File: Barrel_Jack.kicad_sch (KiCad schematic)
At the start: 24 parts, among them J10 Barrel_Jack, J11 Barrel_Jack, J12 Barrel_Jack, J13 Barrel_Jack, J14 Barrel_Jack, J6 Barrel_Jack, J8 Barrel_Jack, J9 Barrel_Jack, U19 34.81-9024, U20 34.81-9024, U21 34.81-9024, U22 34.81-9024, U23 34.81-9024, U24 34.81-9024, U25 34.81-9024, U26 34.81-9024

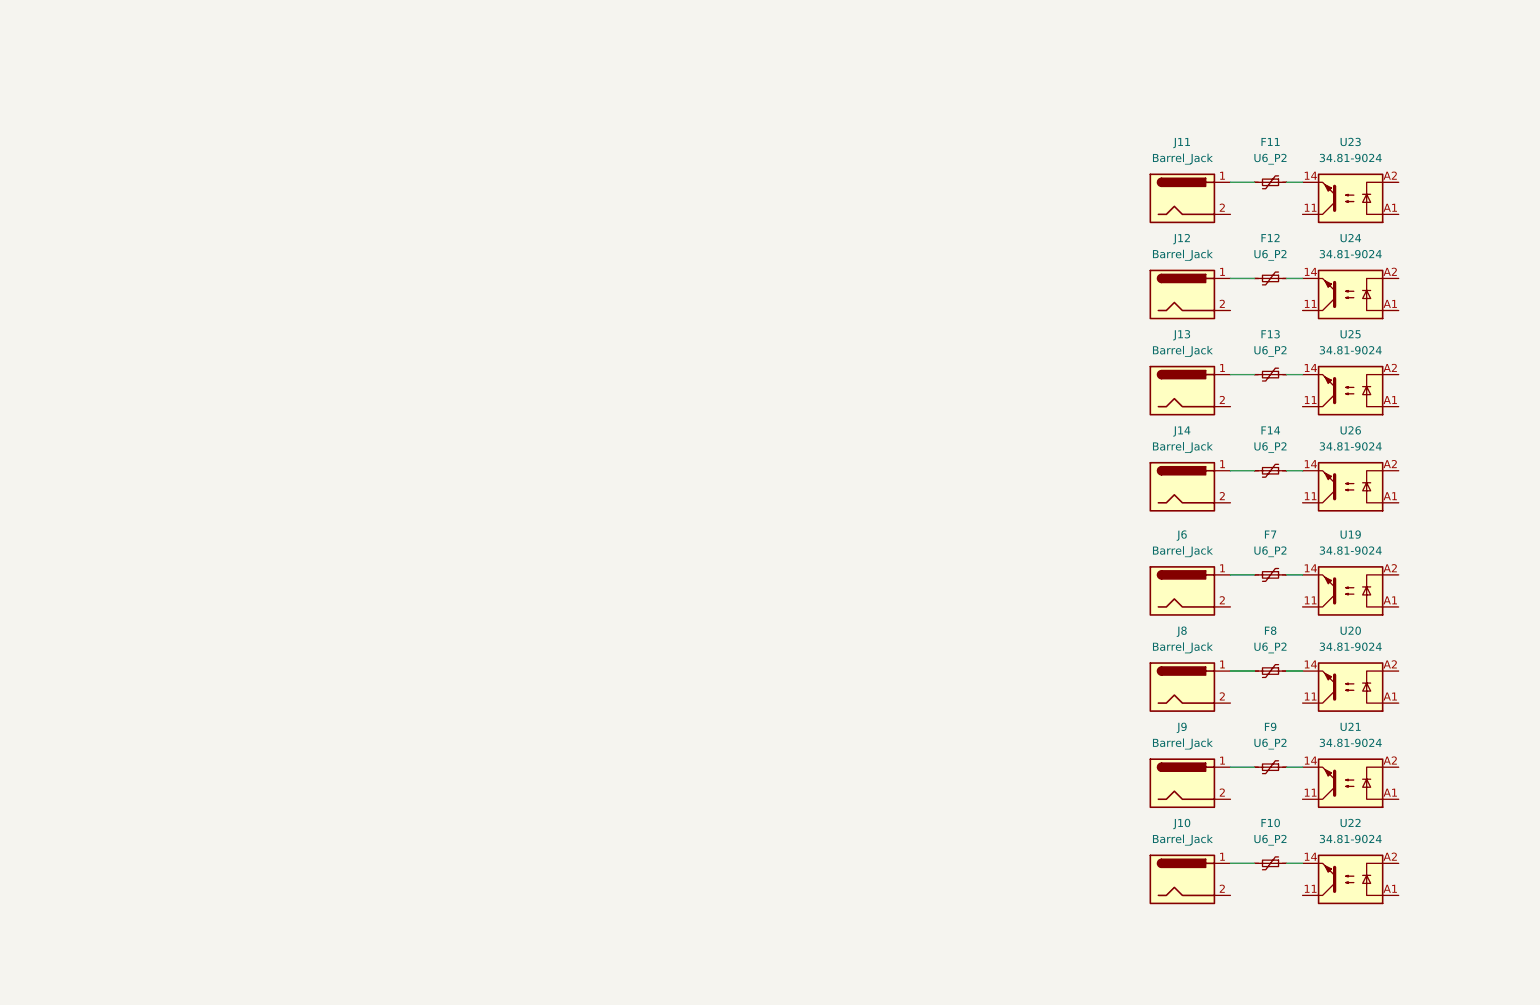
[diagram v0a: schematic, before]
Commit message: barrel jack multiple versions, should be turned into branches
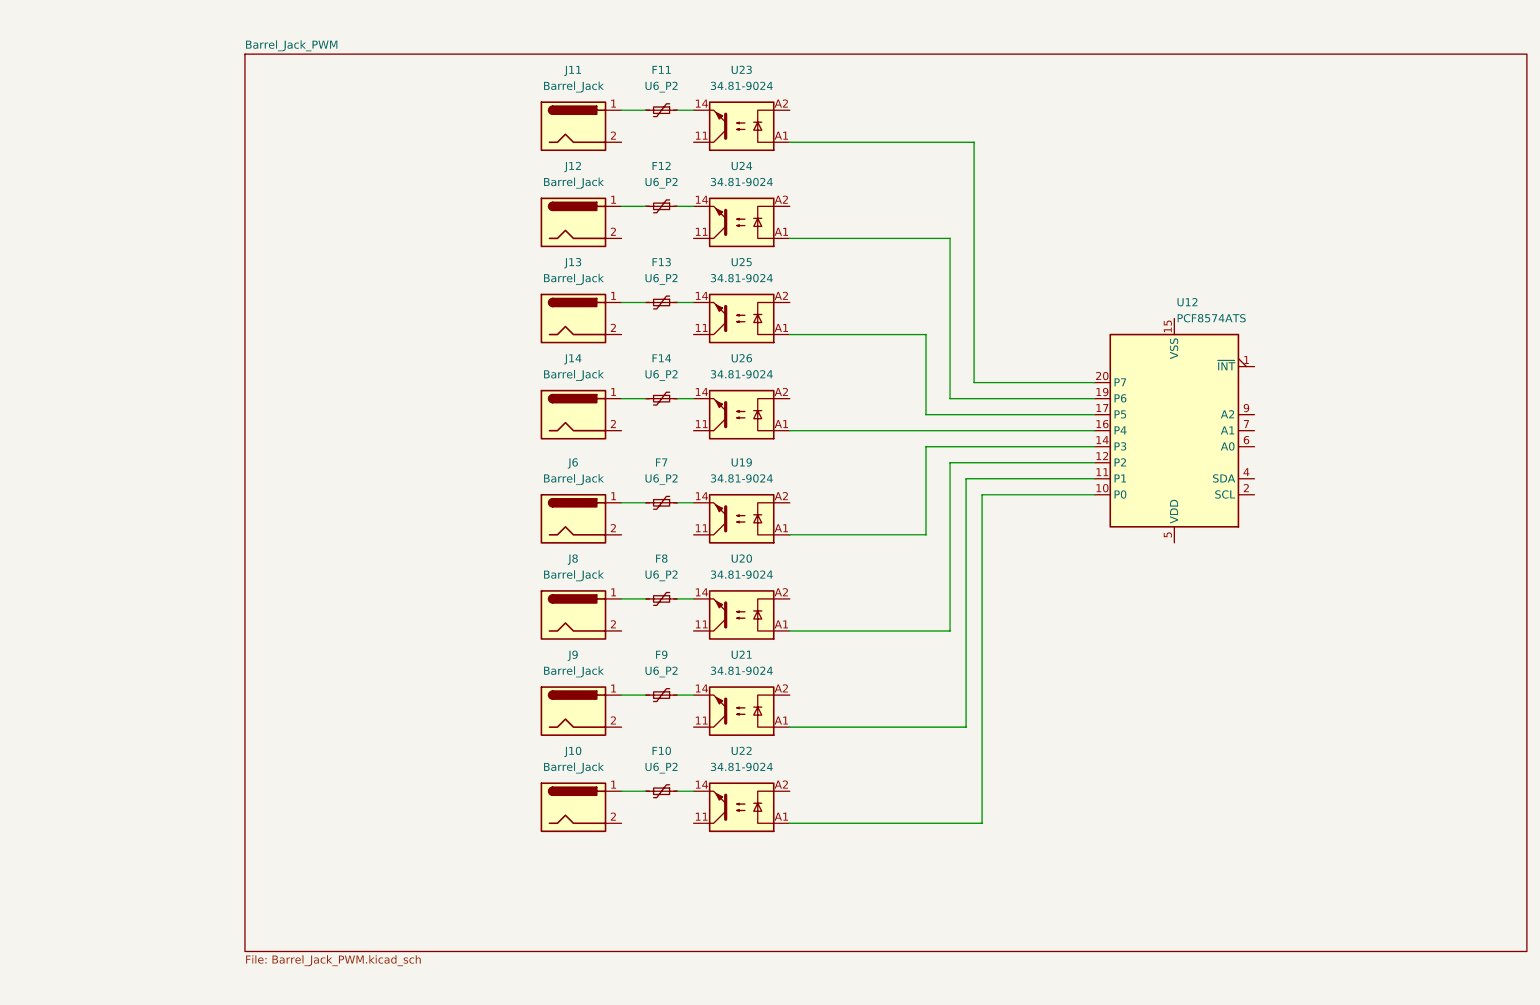
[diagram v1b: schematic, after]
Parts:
- added U12: PCF8574ATS, Package_SO:SSOP-20_4.4x6.5mm_P0.65mm, symbol Interface_Expansion:PCF8574ATS
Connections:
- net at U20.A1: now also U12.12 (P2)
- net at U26.A1: now also U12.16 (P4)
- net at U24.A1: now also U12.19 (P6)
- net at U19.A1: now also U12.14 (P3)
- net at U22.A1: now also U12.10 (P0)
- net at U21.A1: now also U12.11 (P1)
- net at U25.A1: now also U12.17 (P5)
- net at U23.A1: now also U12.20 (P7)
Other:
- added sheet Barrel_Jack_PWM (Barrel_Jack_PWM.kicad_sch)
- moved on the sheet: F10, F11, F12, F13, F14, F7, F8, F9, J10, J11, J12, J13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

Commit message: some additions to barrel jack and its layout
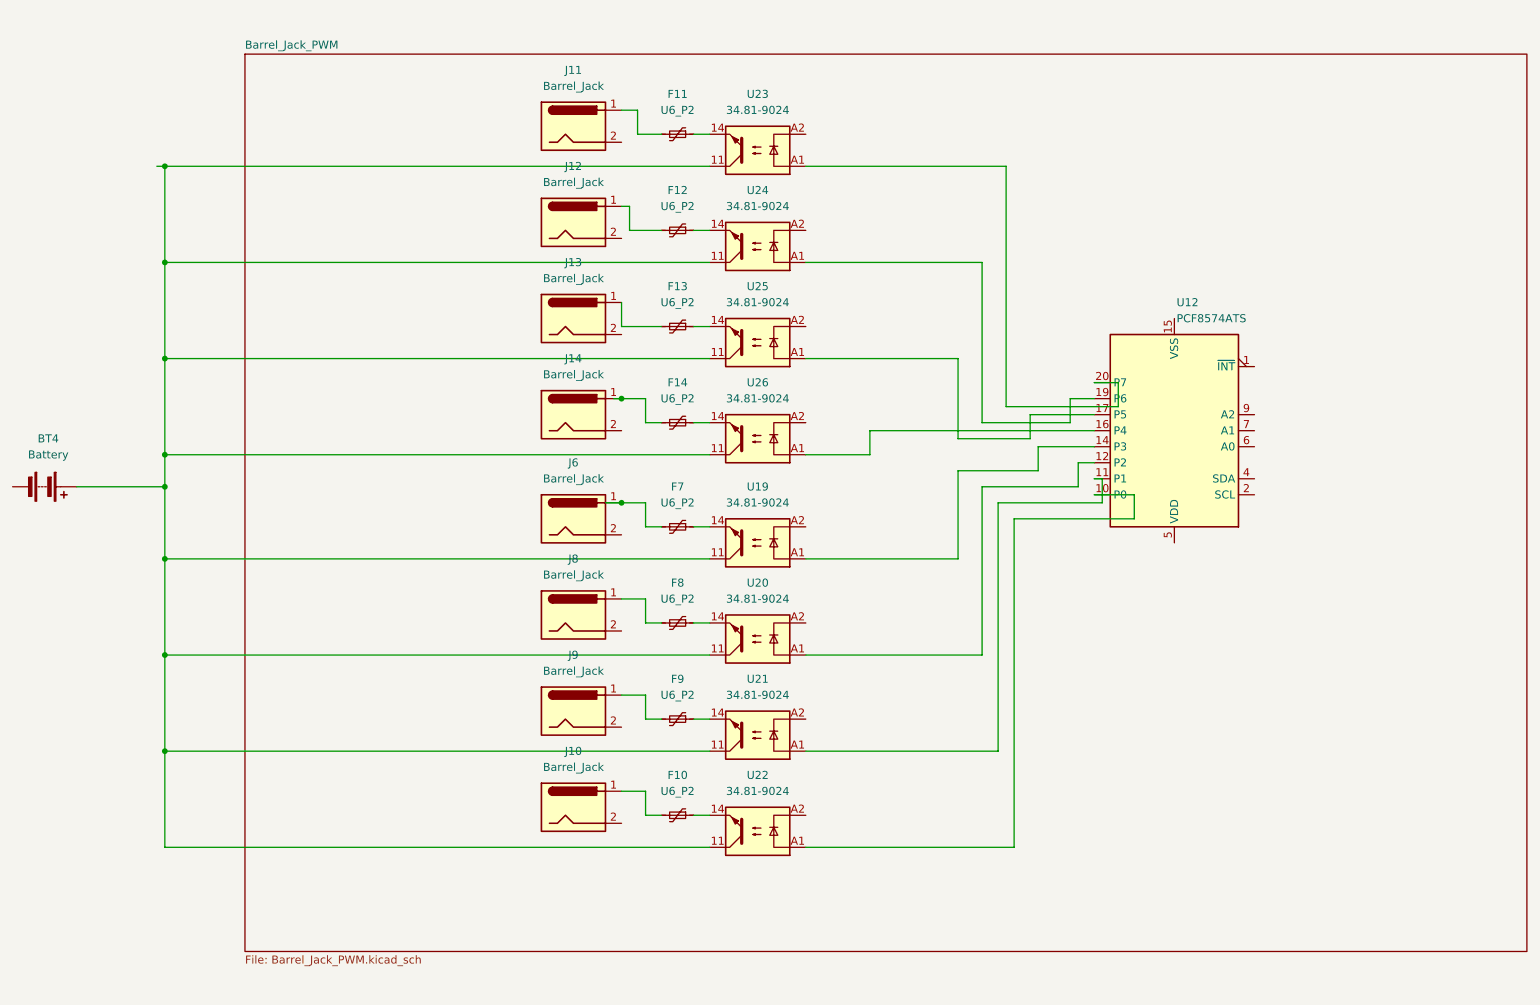
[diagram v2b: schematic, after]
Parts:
- added BT4: Battery, symbol Device:Battery
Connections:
- net at U20.11: now also U19.11, U21.11, U22.11, U23.11, U24.11, U25.11, U26.11, BT4.1 (+)
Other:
- moved on the sheet: F10, F11, F12, F13, F14, F7, F8, F9, U19, U20, U21, U22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
